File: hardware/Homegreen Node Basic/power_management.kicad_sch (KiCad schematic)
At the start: 36 parts, among them J1 USB_B_Micro, J2 USB_A, Q1 WST2011, Q2 BC817DPN, Q3 BC817DPN, U5 MT3608, U6 INA180A2, U7 MT9700

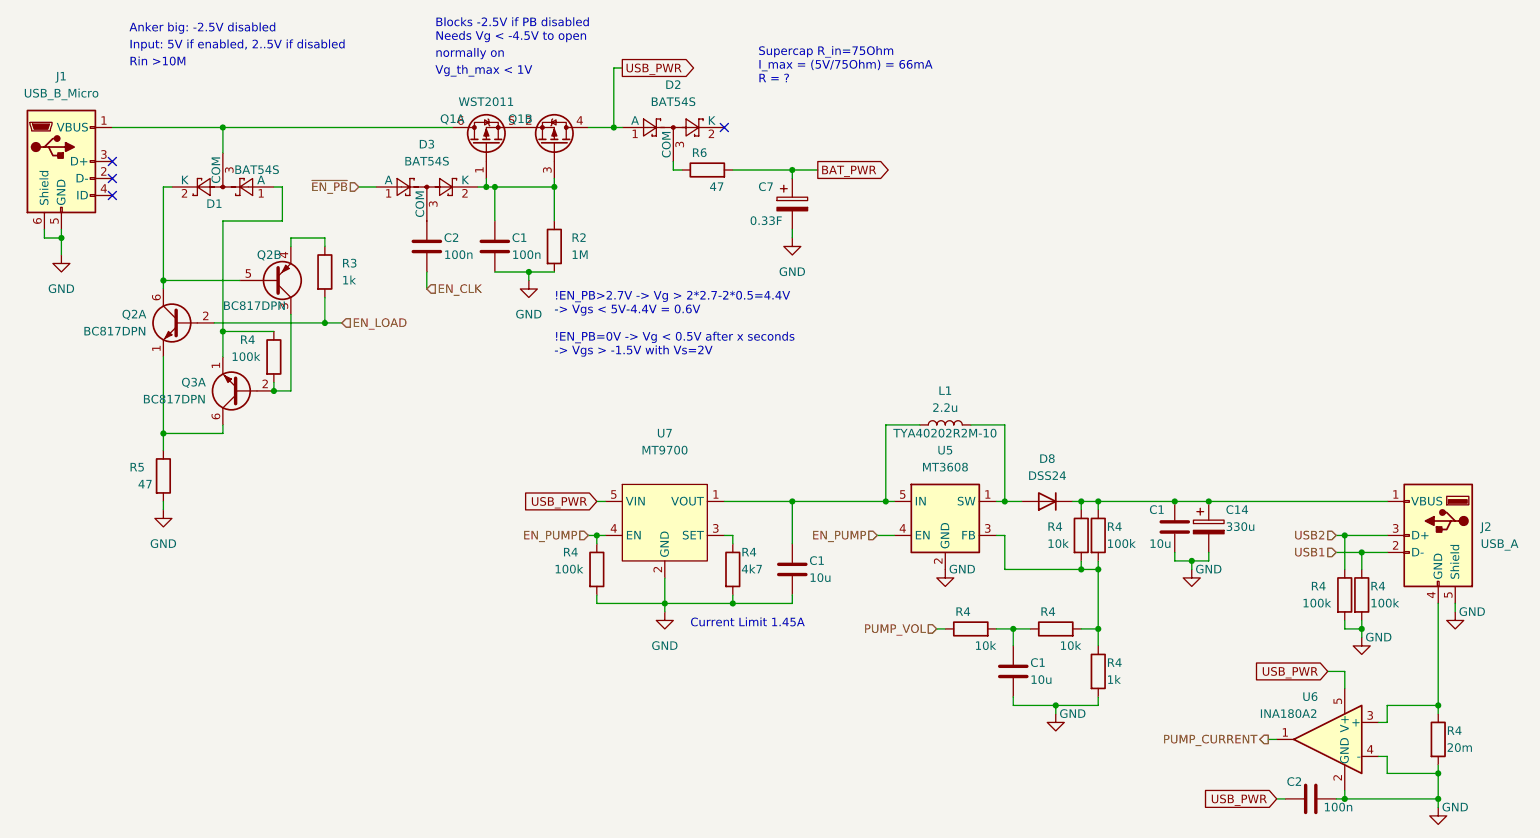
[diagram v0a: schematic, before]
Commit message: - starting with port to atmega328p
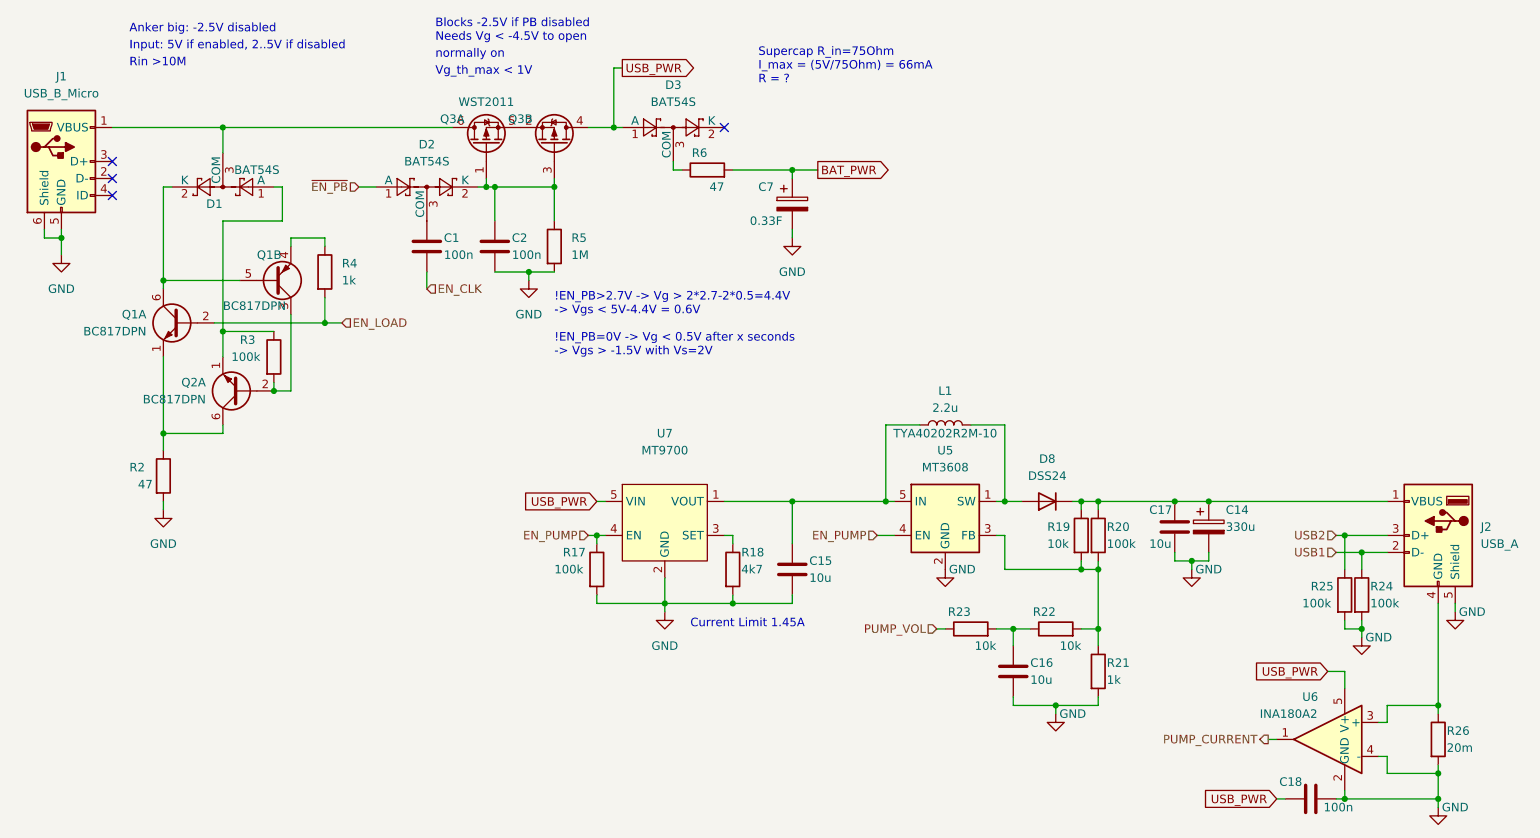
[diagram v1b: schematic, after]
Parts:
- renumbered C2 to C1, C1 to C15, C1 to C16, C1 to C17, C2 to C18, C1 to C2, D3 to D2, D2 to D3, Q2 to Q1, Q3 to Q2, Q1 to Q3, R4 to R17, R4 to R18, R4 to R19, R5 to R2, R4 to R20, R4 to R21, R4 to R22, R4 to R23, R4 to R24, R4 to R25, R4 to R26, R4 to R3, R3 to R4, R2 to R5

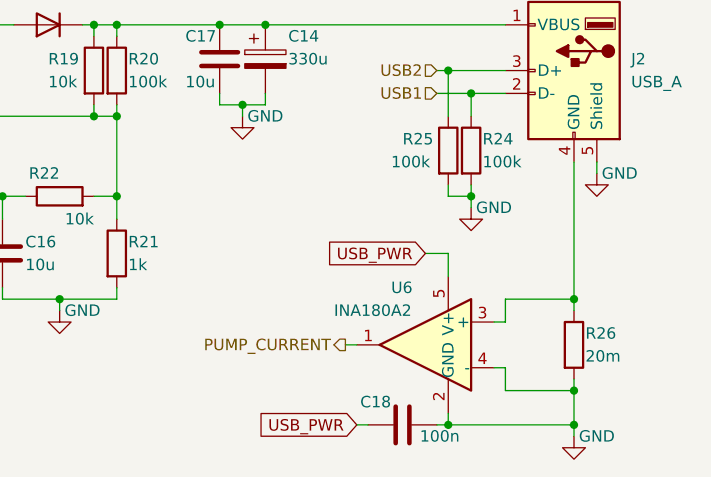
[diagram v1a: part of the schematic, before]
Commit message: update PCB to 1-sided for price estimation
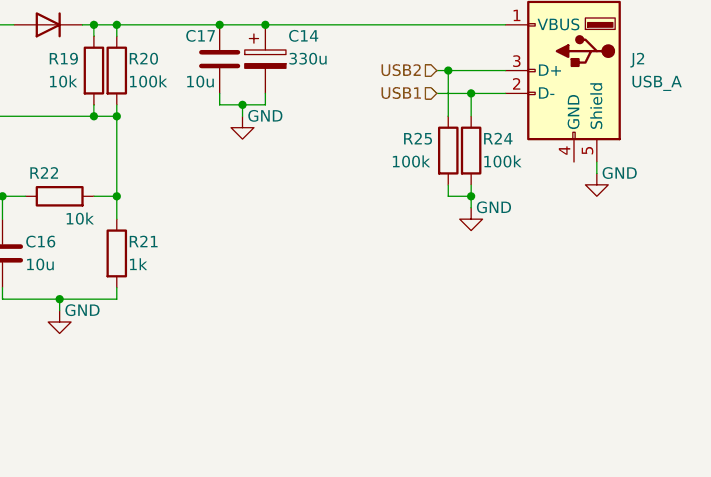
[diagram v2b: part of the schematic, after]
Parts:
- removed C18: 100n, Capacitor_SMD:C_0805_2012Metric, symbol Device:C
- removed R26: 20m, Resistor_SMD:R_0805_2012Metric, symbol Device:R
- removed U6: INA180A2, Package_TO_SOT_SMD:SOT-23-5, symbol Amplifier_Current:INA180A2
